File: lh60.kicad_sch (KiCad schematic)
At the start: 7 parts

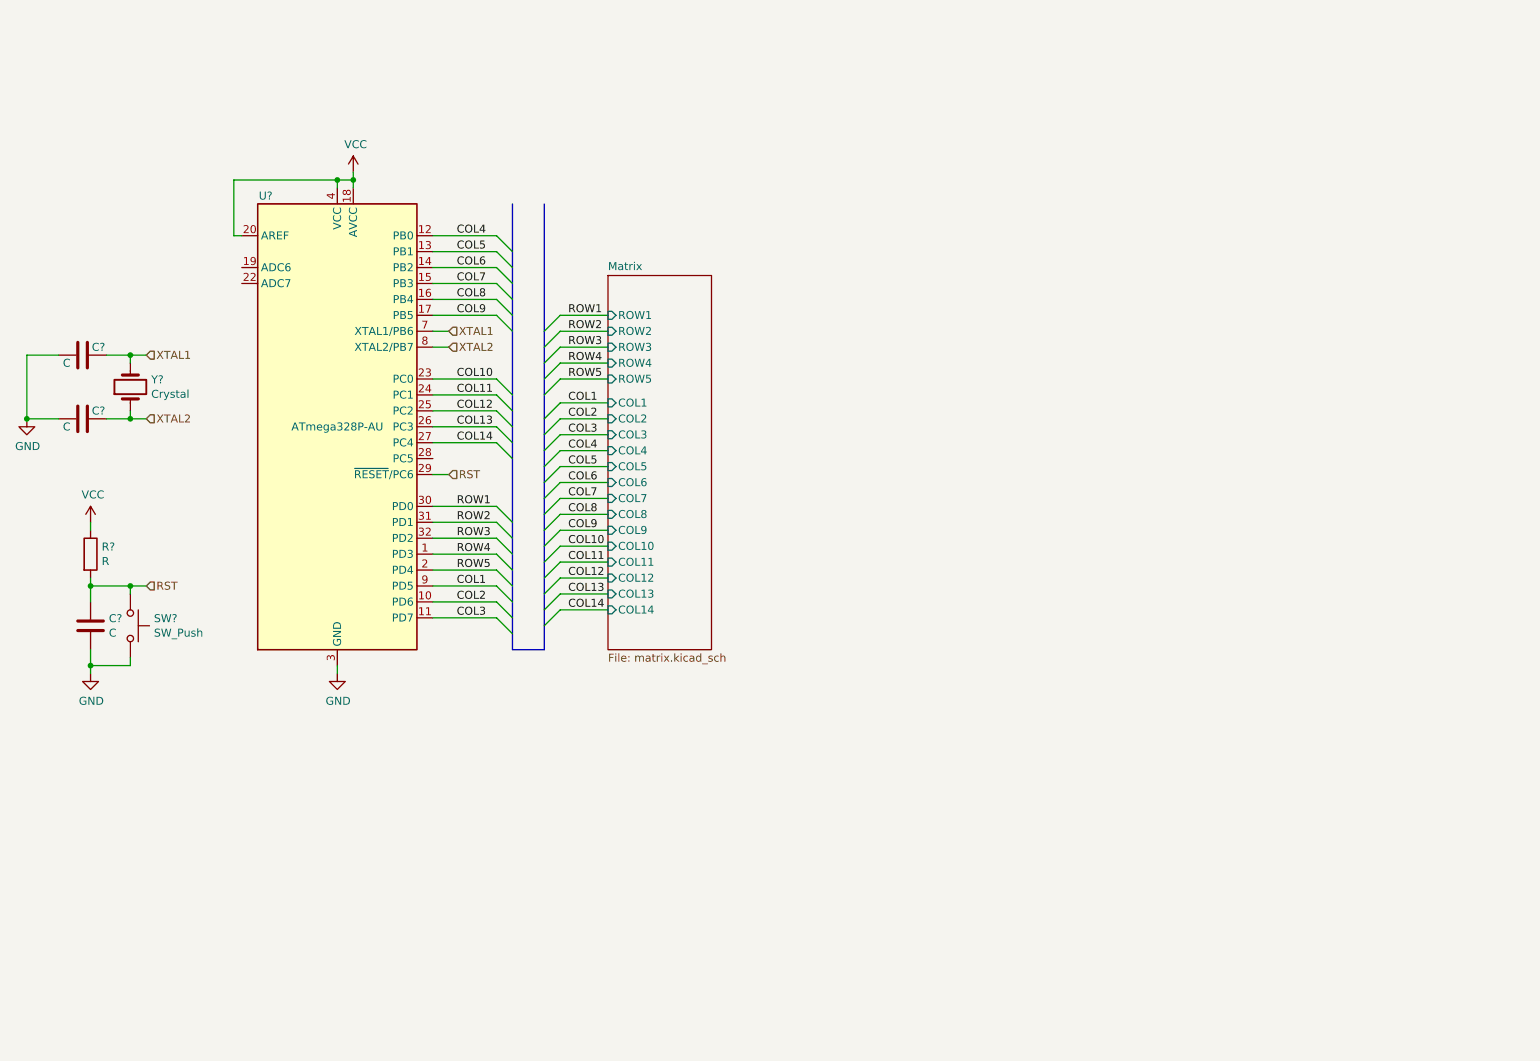
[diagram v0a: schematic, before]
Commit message: 20220325 atmega->stm32
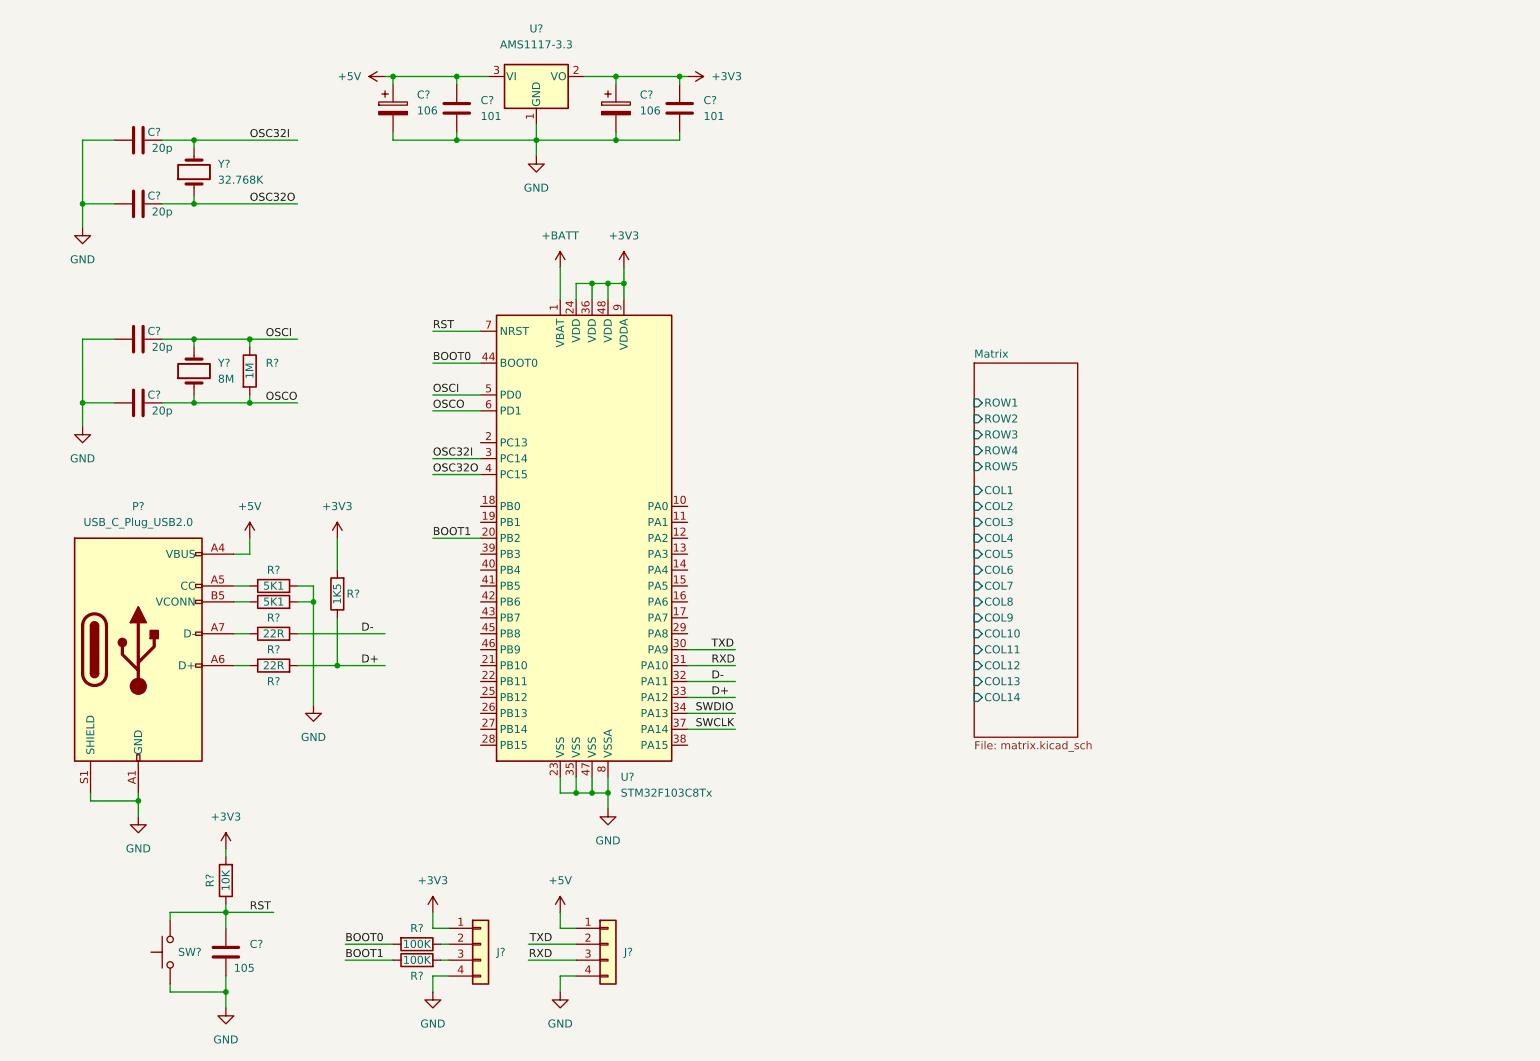
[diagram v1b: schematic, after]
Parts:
- removed C? (x3): C, symbol Device:C
- removed R?: R, symbol Device:R
- removed SW?: SW_Push, symbol Switch:SW_Push
- removed U?: ATmega328P-AU, Package_QFP:TQFP-32_7x7mm_P0.8mm, symbol MCU_Microchip_ATmega:ATmega328P-AU
- removed Y?: Crystal, symbol Device:Crystal
- added C? (x2): 101, symbol Device:C
- added C? (x2): 106, symbol Device:C_Polarized
- added C? (x4): 20p, symbol Device:C
- added C?: 105, symbol Device:C
- added J? (x2): Conn_01x04, symbol Connector_Generic:Conn_01x04
- added P?: USB_C_Plug_USB2.0, symbol Connector:USB_C_Plug_USB2.0
- added R? (x2): 5K1, symbol Device:R
- added R? (x2): 100K, symbol Device:R
- added R? (x2): 22R, symbol Device:R
- added R?: 10K, symbol Device:R
- added R?: 1M, symbol Device:R
- added R?: 1K5, symbol Device:R
- added SW?: SW_Push, symbol Switch:SW_Push
- added U?: STM32F103C8Tx, Package_QFP:LQFP-48_7x7mm_P0.5mm, symbol MCU_ST_STM32F1:STM32F103C8Tx
- added U?: AMS1117-3.3, Package_TO_SOT_SMD:SOT-223-3_TabPin2, symbol Regulator_Linear:AMS1117-3.3
- added Y?: 8M, symbol Device:Crystal
- added Y?: 32.768K, symbol Device:Crystal
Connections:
- net GND: now also C?.1, C?.1, C?.2, C?.2, C?.2, C?.2, C?.2, C?.2, C?.2, J?.4 (Pin_4), J?.4 (Pin_4), P?.A1 (GND), P?.A12 (GND), P?.B1 (GND), P?.B12 (GND), P?.S1 (SHIELD), R?.2, R?.2, SW?.1, U?.1 (GND), U?.23 (VSS), U?.35 (VSS), U?.47 (VSS), U?.8 (VSSA)
- net RST: now also C?.1, R?.1, SW?.2, U?.7 (NRST)
- new net: P?.A5 (CC), R?.1
- new net: J?.3 (Pin_3), R?.2
- new net: P?.A7 (D-), R?.1
- new net: J?.2 (Pin_2), R?.1
- new net: P?.A6 (D+), R?.1
- new net: P?.B5 (VCONN), R?.1
- new net +3V3: C?.1, C?.1, J?.1 (Pin_1), R?.2, R?.2, U?.2 (VO), U?.24 (VDD), U?.36 (VDD), U?.48 (VDD), U?.9 (VDDA)
- new net +5V: C?.1, C?.1, J?.1 (Pin_1), P?.A4 (VBUS), P?.A9 (VBUS), P?.B4 (VBUS), P?.B9 (VBUS), U?.3 (VI)
- new net +BATT: U?.1 (VBAT)
- new net BOOT0: R?.2, U?.44 (BOOT0)
- new net BOOT1: R?.1, U?.20 (PB2)
- new net D+: R?.1, R?.2, U?.33 (PA12)
- new net D-: R?.2, U?.32 (PA11)
- new net OSC32I: C?.1, U?.3 (PC14), Y?.2
- new net OSC32O: C?.2, U?.4 (PC15), Y?.1
- new net OSCI: C?.1, R?.1, U?.5 (PD0), Y?.2
- new net OSCO: C?.2, R?.2, U?.6 (PD1), Y?.1
- new net RXD: J?.3 (Pin_3), U?.31 (PA10)
- new net SWCLK: U?.37 (PA14)
- new net SWDIO: U?.34 (PA13)
- new net TXD: J?.2 (Pin_2), U?.30 (PA9)

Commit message: sch fin
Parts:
- removed Y?: 8M, symbol Device:Crystal
- added C10, C11, C12, C13: 104, Capacitor_SMD:C_0603_1608Metric_Pad1.08x0.95mm_HandSolder, symbol Device:C
- added Y2: 8M, Crystal:Crystal_SMD_3225-4Pin_3.2x2.5mm_HandSoldering, symbol Device:Crystal_GND24
- C1, C2, C3, C4, C5, C6, C7, C8, C9: renamed from C?; footprint (none) -> Capacitor_SMD:C_0603_1608Metric_Pad1.08x0.95mm_HandSolder
- J1, J2: renamed from J?; footprint (none) -> Connector_PinHeader_1.27mm:PinHeader_1x04_P1.27mm_Vertical
- P1: renamed from P?; footprint (none) -> Connector_USB:USB_C_Receptacle_HRO_TYPE-C-31-M-12
- R1, R2, R3, R4, R5, R6, R7, R8, R9: renamed from R?; footprint (none) -> Resistor_SMD:R_0603_1608Metric_Pad0.98x0.95mm_HandSolder
- SW1: renamed from SW?; footprint (none) -> Button_Switch_SMD:SW_SPST_FSMSM
- Y1: renamed from Y?; footprint (none) -> Crystal:Crystal_SMD_3215-2Pin_3.2x1.5mm
- gave numbers to parts that had none: 2
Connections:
- net +3V3: now also C10.1, C11.1, C12.1, C13.1
- net GND: now also C10.2, C11.2, C12.2, C13.2, Y2.2, Y2.4
- net OSCI: now also Y2.3
- net OSCO: now also Y2.1
- net COL1: now reaches U2.10 (PA0)
- net COL2: now reaches U2.11 (PA1)
- net COL3: now reaches U2.12 (PA2)
- net COL4: now reaches U2.13 (PA3)
- net COL5: now reaches U2.14 (PA4)
- net COL6: now reaches U2.15 (PA5)
- net COL7: now reaches U2.16 (PA6)
- net COL8: now reaches U2.17 (PA7)
- net COL9: now reaches U2.18 (PB0)
- net COL10: now reaches U2.19 (PB1)
- net COL11: now reaches U2.21 (PB10)
- net COL12: now reaches U2.22 (PB11)
- net COL13: now reaches U2.25 (PB12)
- net COL14: now reaches U2.26 (PB13)
- net ROW1: now reaches U2.38 (PA15)
- net ROW2: now reaches U2.39 (PB3)
- net ROW3: now reaches U2.40 (PB4)
- net ROW4: now reaches U2.41 (PB5)
- net ROW5: now reaches U2.42 (PB6)
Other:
- moved on the sheet: C1, C2, C3, C4, C5, C6, C7, C8, C9, J1, J2, P1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

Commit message: 20220326 pcb init
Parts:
- C5, C7: footprint Capacitor_SMD:C_0603_1608Metric_Pad1.08x0.95mm_HandSolder -> Capacitor_SMD:C_1206_3216Metric_Pad1.33x1.80mm_HandSolder

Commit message: 20220326 fin
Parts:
- removed J1, J2: Conn_01x04, Connector_PinHeader_1.27mm:PinHeader_1x04_P1.27mm_Vertical, symbol Connector_Generic:Conn_01x04
- added J1: Conn_01x03_Female, Connector_PinHeader_2.54mm:PinHeader_1x03_P2.54mm_Vertical, symbol Connector:Conn_01x03_Female
- added J3, J5: Conn_01x02_Female, Connector_PinHeader_2.54mm:PinHeader_1x02_P2.54mm_Vertical, symbol Connector:Conn_01x02_Female
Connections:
- net +3V3: now also J1.2 (Pin_2)
- net +5V: now also J1.1 (Pin_1)
- net GND: now also J1.3 (Pin_3)
- net RXD: now also J5.2 (Pin_2)
- net TXD: now also J5.1 (Pin_1)
- net at R9.2: now also J3.2 (Pin_2)
- net at R8.1: now also J3.1 (Pin_1)

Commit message: 20220401 sch 2.0
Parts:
- removed C6, C8: 101, Capacitor_SMD:C_0603_1608Metric_Pad1.08x0.95mm_HandSolder, symbol Device:C
- removed P1: USB_C_Plug_USB2.0, Connector_USB:USB_C_Receptacle_HRO_TYPE-C-31-M-12, symbol Connector:USB_C_Plug_USB2.0
- added J2: USB_C_Receptacle_USB2.0, symbol Connector:USB_C_Receptacle_USB2.0
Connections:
- net +5V: now also J2.A4 (VBUS), J2.A9 (VBUS), J2.B4 (VBUS), J2.B9 (VBUS)
- net BOOT0: now also J3.1 (Pin_1)
- net BOOT1: now also J3.2 (Pin_2)
- net D+: now also J2.A6 (D+), J2.B6 (D+); no longer U2.33 (PA12)
- net D-: now also J2.A7 (D-), J2.B7 (D-); no longer U2.32 (PA11)
- net GND: now also R8.1, R9.2, J2.A1 (GND), J2.A12 (GND), J2.B1 (GND), J2.B12 (GND), J2.S1 (SHIELD)
- net at R2.1: now also J2.A5 (CC1)
- net UD-: now reaches R4.1
- net UD-: now also U2.32 (PA11)
- net UD+: now reaches R5.1
- net UD+: now also U2.33 (PA12)
- net at R3.1: now also J2.B5 (CC2)
- no-connect marks 0 -> 2
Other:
- moved on the sheet: C1, C10, C11, C12, C13, C2, C3, C4, C7, C9, J1, J3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

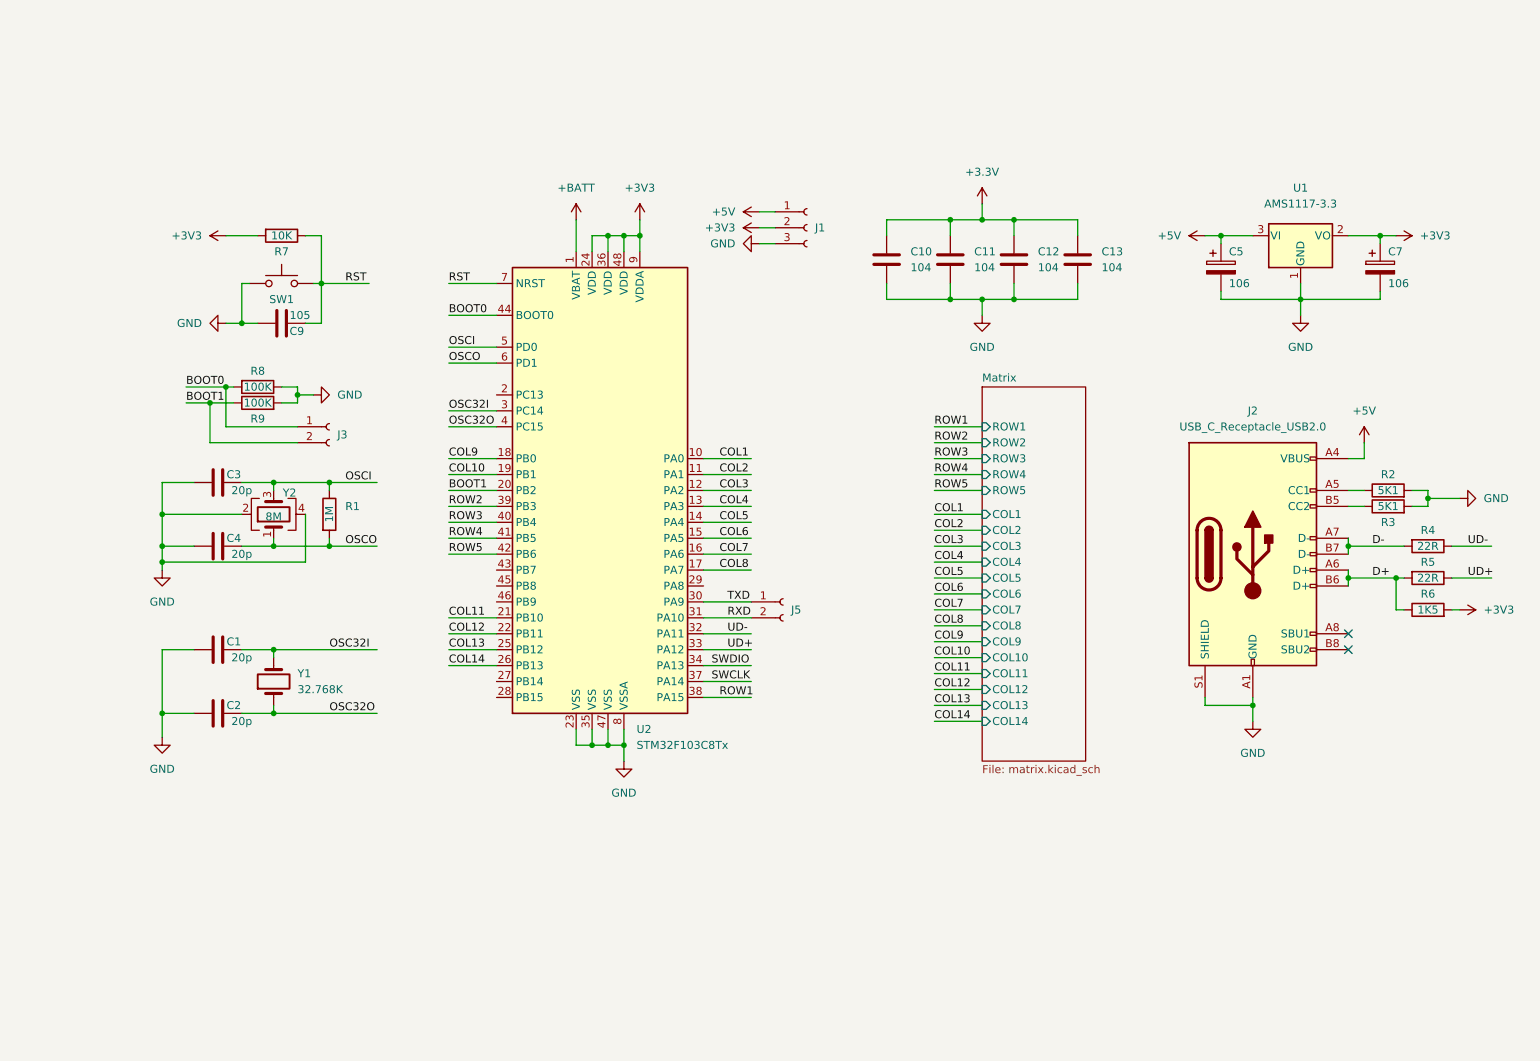
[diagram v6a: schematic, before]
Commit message: alter usbc to jump connecter
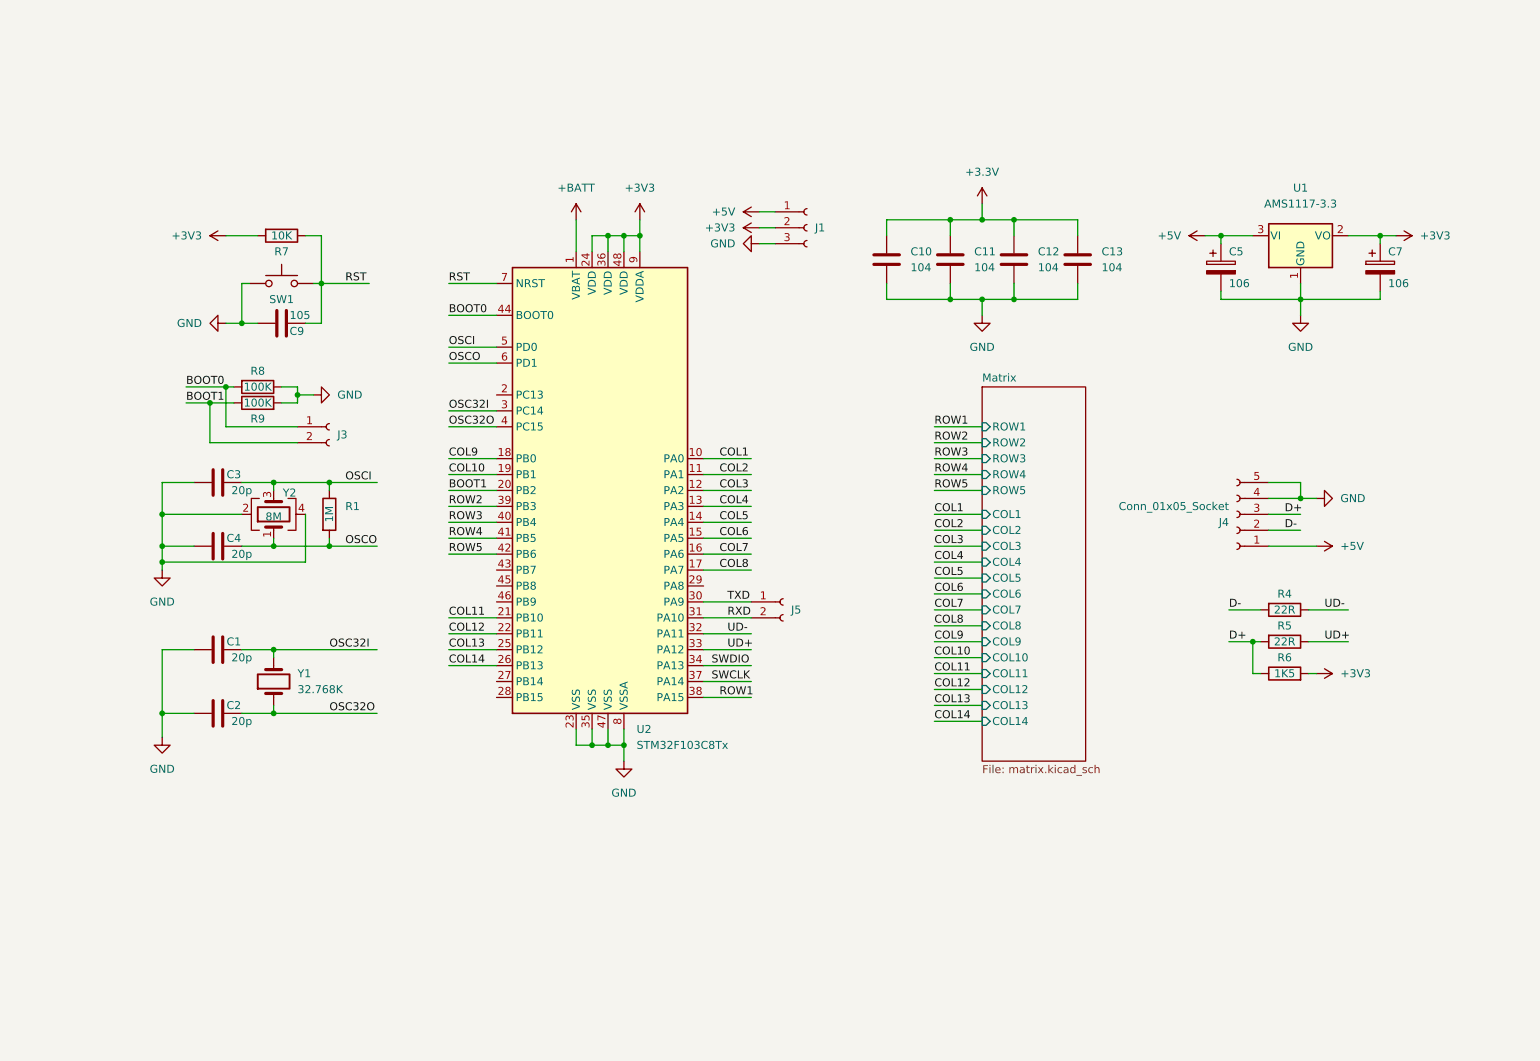
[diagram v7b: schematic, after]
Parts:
- removed J2: USB_C_Receptacle_USB2.0, symbol Connector:USB_C_Receptacle_USB2.0
- removed R2, R3: 5K1, Resistor_SMD:R_0603_1608Metric_Pad0.98x0.95mm_HandSolder, symbol Device:R
- added J4: Conn_01x05_Socket, USB-C:Connector-1.25-5AWT-Horizontal, symbol Connector:Conn_01x05_Socket
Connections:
- net +5V: now also J4.1 (Pin_1)
- net D+: now also J4.3 (Pin_3)
- net D-: now also J4.2 (Pin_2)
- net GND: now also J4.4 (Pin_4), J4.5 (Pin_5)
- no-connect marks 2 -> 0
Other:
- moved on the sheet: R4, R5, R6
